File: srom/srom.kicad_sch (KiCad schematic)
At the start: 21 parts, among them J1 Conn_01x03_Female, J101 Conn_01x06_Female, Q1 PMBT2222A, U1 4075, U101 74LS245, U4 74LS245, U5 Pico-1 ROM

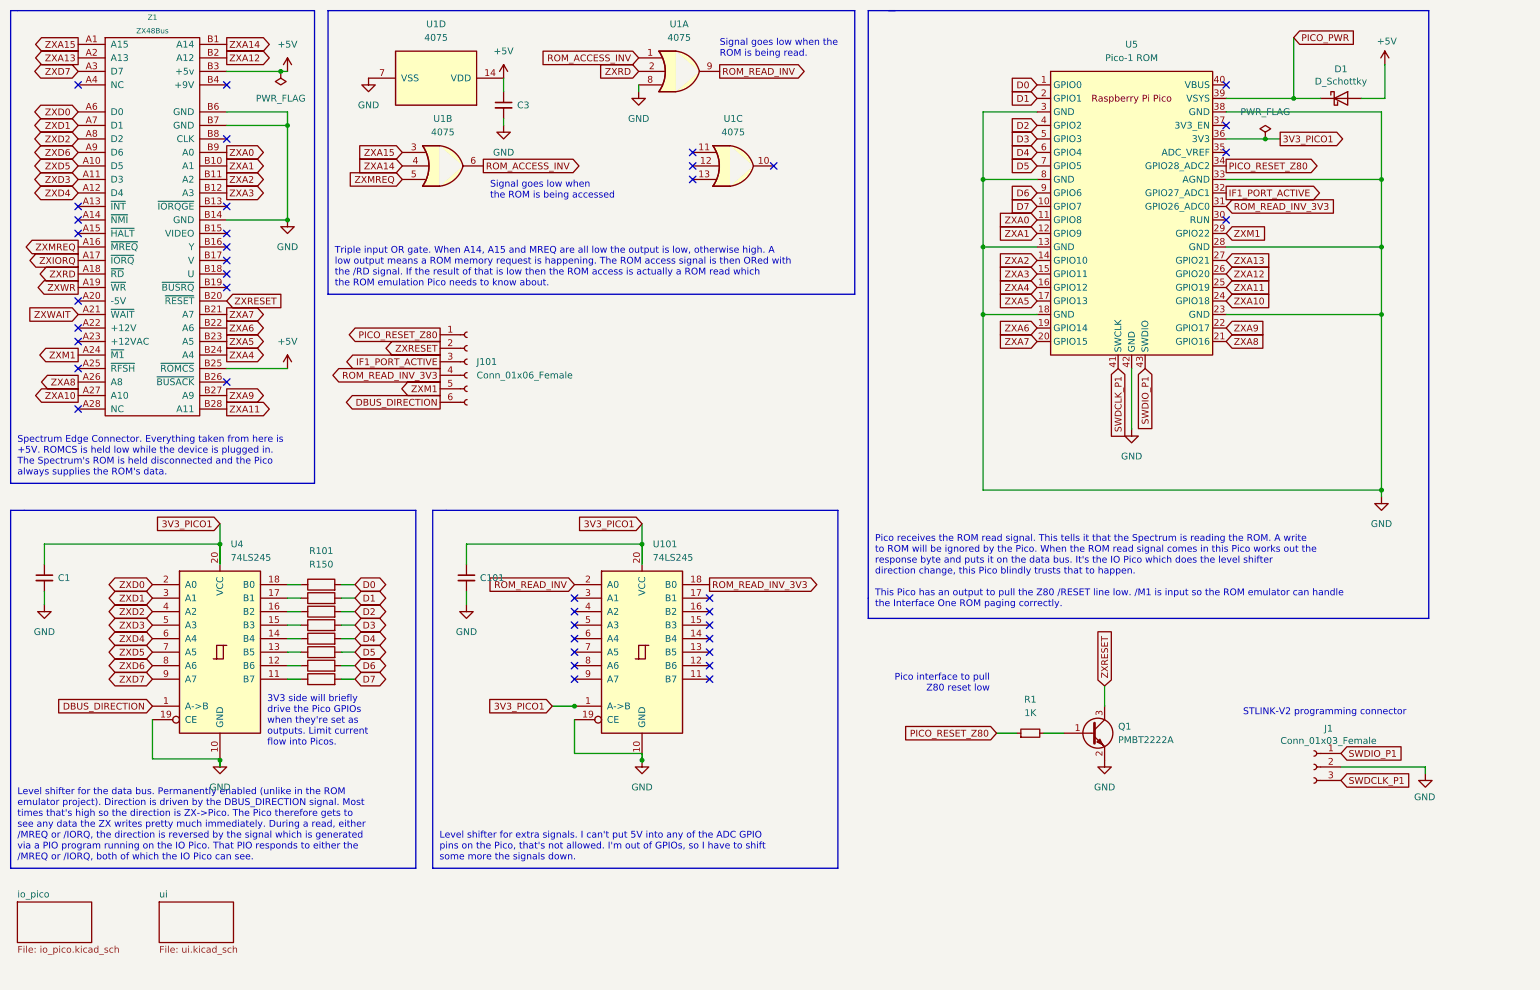
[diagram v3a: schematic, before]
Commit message: add rear edge schematic, RUN switch, ROMCS2 signal
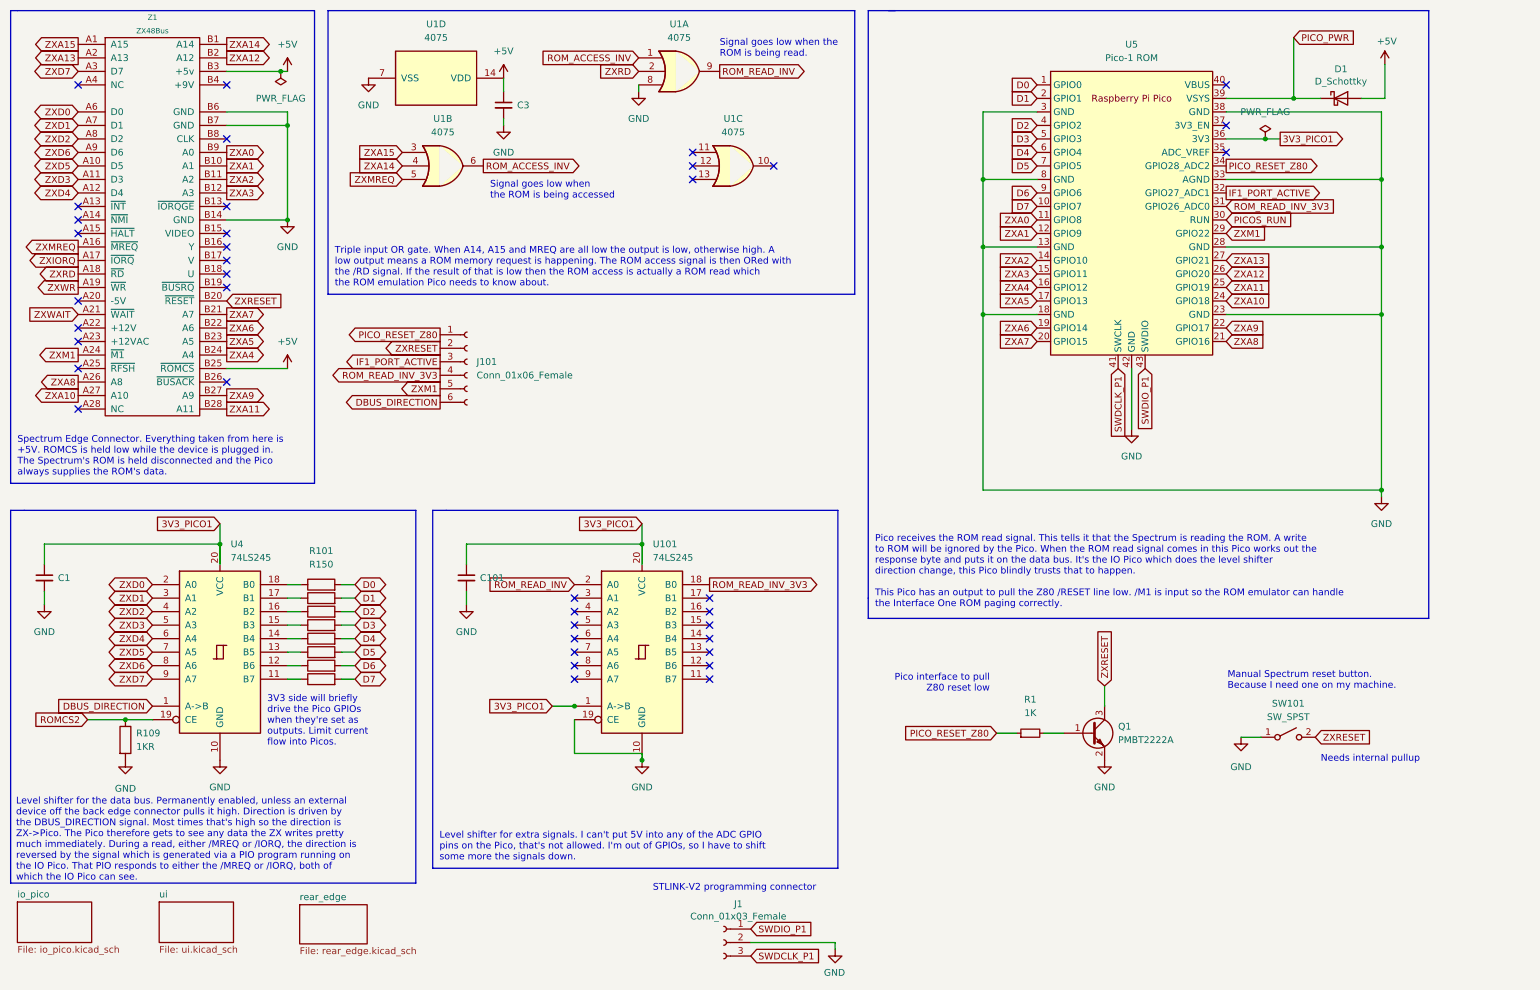
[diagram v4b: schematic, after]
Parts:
- added R109: 1KR, Resistor_SMD:R_1206_3216Metric_Pad1.30x1.75mm_HandSolder, symbol Device:R
- added SW101: SW_SPST, Button_Switch_THT:SW_Tactile_SKHH_Angled, symbol Switch:SW_SPST
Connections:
- net GND: now also R109.2, SW101.1 (A); no longer U4.19 (CE)
- net ZXRESET: now also SW101.2 (B)
- net PICOS_RUN: now reaches U5.30 (RUN)
- new net ROMCS2: R109.1, U4.19 (CE)
- no-connect marks 40 -> 39
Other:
- added sheet rear_edge (rear_edge.kicad_sch)
- note added: "Level shifter for the data bus. Permanently enabled, unless an external device off the back edge connector pulls it high. Direction is driven by the DBUS_DIRECTION signal. Most times that's high so the direction is ZX->Pico. The Pico therefore gets to see any data the ZX writes pretty much immediately. During a read, either /MREQ or /IORQ, the direction is reversed by the signal which is generate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"
- note added: "Manual Spectrum reset button. Because I need one on my machine."
- note added: "Needs internal pullup"
- note removed: "Level shifter for the data bus. Permanently enabled (unlike in the ROM emulator project). Direction is driven by the DBUS_DIRECTION signal. Most times that's high so the direction is ZX->Pico. The Pico therefore gets to see any data the ZX writes pretty much immediately. During a read, either /MREQ or /IORQ, the direction is reversed by the signal which is generated via a PIO program running on t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"
- moved on the sheet: J1

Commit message: remove test point connectors, no needed on next board (famous last words)
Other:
- note added: "EXCLUDED FROM BOARD"
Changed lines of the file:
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@@
+    (effects (font (size 1.27 1.27)) (justify left bottom))
+  )
+  (text "EXCLUDED FROM BOARD" (at 85.09 94.488 0)
+    (effects (font (size 1.27 1.27)) (justify left bottom))
+  )
+  (text "EXCLUDED FROM BOARD" (at 130.048 196.596 0)
     (effects (font (size 1.27 1.27)) (justify left bottom))
   )
@@
   )
   (symbol (lib_id "Connector:Conn_01x06_Female") (at 99.822 81.28 0) (unit 1)
-    (in_bom yes) (on_board yes) (fields_autoplaced)
+    (in_bom yes) (on_board no) (fields_autoplaced)
     (property "Reference" "J101" (id 0) (at 101.6 81.2799 0)
       (effects (font (size 1.27 1.27)) (justify left))
@@
   )
   (symbol (lib_id "Connector:Conn_01x03_Female") (at 148.082 190.5 0) (mirror y) (unit 1)
-    (in_bom yes) (on_board yes)
+    (in_bom yes) (on_board no)
     (property "Reference" "J1" (id 0) (at 150.8252 183.261 0))
     (property "Value" "Conn_01x03_Female" (id 1) (at 150.8252 185.5724 0))
@@
       (reference "J202") (unit 1) (value "Conn_01x06_Female") (footprint "Connector_PinHeader_2.54mm:PinHeader_1x06_P2.54mm_Vertical")
     )
-    (path "/acda4c69-0a65-473b-ab4f-e765252d7da2/cb841d88-a75c-4f80-ba44-02c4407c29e0"
-      (reference "J302") (unit 1) (value "Conn_01x04_Female") (footprint "Connector_PinHeader_2.54mm:PinHeader_1x04_P2.54mm_Vertical")
+    (path "/acda4c69-0a65-473b-ab4f-e765252d7da2/2e0e69b0-32c8-43e8-a14f-982c095ddf69"
+      (reference "J301") (unit 1) (value "Conn_01x10_Female") (footprint "")
     )
     (path "/acda4c69-0a65-473b-ab4f-e765252d7da2/93673449-babe-4629-b5c4-4cd05c3c812a"
       (reference "J303") (unit 1) (value "Conn_01x03_Female") (footprint "Connector_PinHeader_2.54mm:PinHeader_1x03_P2.54mm_Vertical")
     )
-    (path "/acda4c69-0a65-473b-ab4f-e765252d7da2/b286c952-0d40-46dc-91e0-859f779bcde5"
-      (reference "J304") (unit 1) (value "Conn_01x06_Female") (footprint "Connector_PinHeader_2.54mm:PinHeader_1x06_P2.54mm_Vertical")
+    (path "/acda4c69-0a65-473b-ab4f-e765252d7da2/3606aacd-196f-47ae-a3bb-b12457540919"
+      (reference "J?") (unit 1) (value "Conn_01x06_Female") (footprint "")
     )
     (path "/e33c0819-efed-4286-8863-9252958751f9"

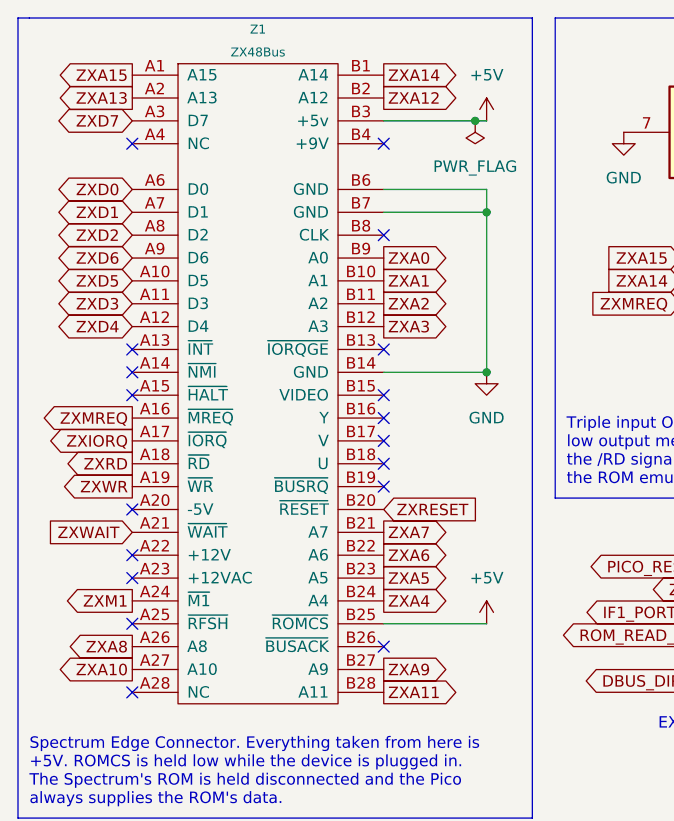
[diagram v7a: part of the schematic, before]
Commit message: board layout work, 4 layers
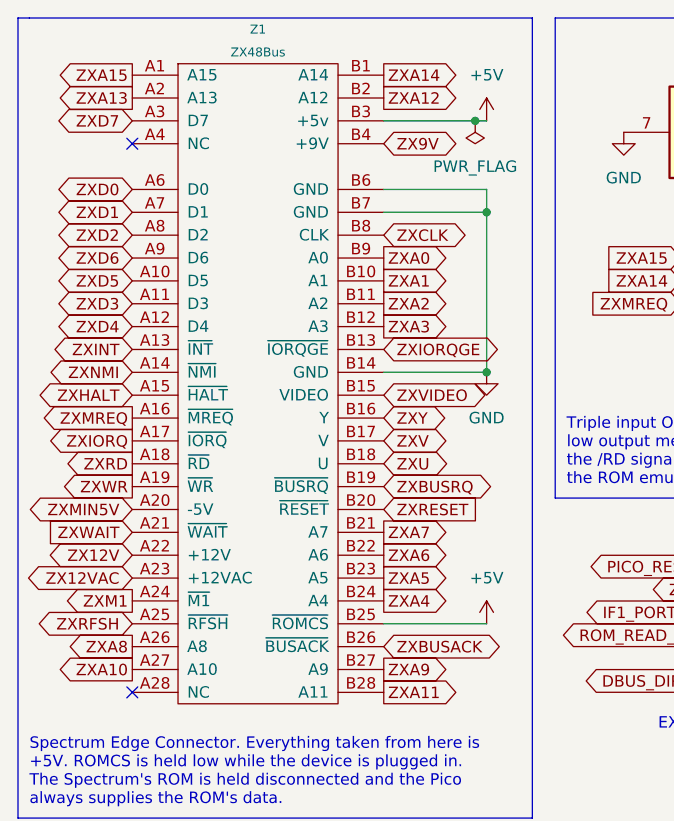
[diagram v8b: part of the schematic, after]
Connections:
- net ZXINT: now reaches Z1.A13 (~{INT})
- net ZXNMI: now reaches Z1.A14 (~{NMI})
- net ZXHALT: now reaches Z1.A15 (~{HALT})
- net ZXMIN5V: now reaches Z1.A20 (-5V)
- net ZX12V: now reaches Z1.A22 (+12V)
- net ZX12VAC: now reaches Z1.A23 (+12VAC)
- net ZXRFSH: now reaches Z1.A25 (~{RFSH})
- net ZXIORQGE: now reaches Z1.B13 (~{IORQGE})
- net ZXVIDEO: now reaches Z1.B15 (VIDEO)
- net ZXY: now reaches Z1.B16 (Y)
- net ZXV: now reaches Z1.B17 (V)
- net ZXU: now reaches Z1.B18 (U)
- net ZXBUSRQ: now reaches Z1.B19 (~{BUSRQ})
- net ZXBUSACK: now reaches Z1.B26 (~{BUSACK})
- net ZX9V: now reaches Z1.B4 (+9V)
- net ZXCLK: now reaches Z1.B8 (CLK)
- no-connect marks 39 -> 23
